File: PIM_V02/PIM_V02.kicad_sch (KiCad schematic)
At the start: 161 parts, among them J1 Conn_01x06, J10 Conn_02x08_Odd_Even, J4 USB_C_Receptacle_USB2.0_14P, J5 Conn_01x04, J6 Conn_01x04, J8 Conn_01x02, J9 Conn_02x08_Odd_Even, Q1 SQJ407EP-T1_GE3, Q2 PMOS, Q3 PMOS, Q4 NMOS, Q5 2N7002, SW1 SW_Push, U1 TPS259541DSGR, U11 AP2112K-3.3, U13 MT29F1G01ABAFDWB-IT_F, U14 MB85RS256B, U15 ICE40UP5K-SG48I, U2 USBLC6-2SC6, U3 STM32H7A3VITx, Y1 Crystal_GND24_Small

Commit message: pc104 outline, nearly done with layout, managed to keep it at 4 layers but the traces became quite messy; still need to do an in depth review to ensure i havent cut across any zones unknowingly; also there are still DRC errors that i need to work through - but all nets are connected !
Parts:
- removed J10, J9: Conn_02x08_Odd_Even, Connector_PinHeader_2.54mm:PinHeader_2x08_P2.54mm_Vertical, symbol Connector_Generic:Conn_02x08_Odd_Even
- removed J8: Conn_01x02, Connector_PinHeader_2.54mm:PinHeader_1x02_P2.54mm_Vertical, symbol Connector_Generic:Conn_01x02
- removed Q5: 2N7002, Package_TO_SOT_SMD:SOT-23, symbol Transistor_FET:2N7002
- removed R57, R58: 4.7kR, Resistor_SMD:R_0603_1608Metric, symbol Device:R_Small
- removed TP10, TP19, TP20, TP9: TestPoint, TestPoint:TestPoint_Pad_D1.0mm, symbol Connector:TestPoint
- removed U1: TPS259541DSGR, CustomFootprints:DSG0008A, symbol Custom_Components:TPS259573DSGR
- added D16: BAS316, Diode_SMD:D_SOD-323, symbol Diode:BAS316
- added J12, J13: Conn_01x12, CustomFootprints:5040501291, symbol Connector_Generic:Conn_01x12
- added J14: Conn_01x04, Connector_Molex:Molex_PicoBlade_53261-0471_1x04-1MP_P1.25mm_Horizontal, symbol Connector_Generic:Conn_01x04
- added R145, R149: 10kR, Resistor_SMD:R_0603_1608Metric, symbol Device:R_Small
- added R146: 33R, Resistor_SMD:R_0402_1005Metric, symbol Device:R_Small
- added R147, R148: 33R, Resistor_SMD:R_0603_1608Metric, symbol Device:R_Small
- added TP21, TP25: TestPoint, TestPoint:TestPoint_Pad_D1.0mm, symbol Connector:TestPoint
- added U1: TPS259540DSGR, CustomFootprints:DSG0008A, symbol Custom_Components:TPS259540DSGR
- R100, R102, R103, R104, R105, R106, R107, R108, R109, R118, R119, R120, R121, R99: footprint Resistor_SMD:R_0603_1608Metric -> Resistor_SMD:R_0402_1005Metric; MPN ERJ-3EKF33R0V -> ERJ-2RKF33R0X; PD RES SMD 33 OHM 1% 1/10W 0603 -> RES SMD 33 OHM 1% 1/10W 0402
- R110, R111, R112, R113, R114, R115, R116, R117, R123, R124, R125, R126, R127: footprint Resistor_SMD:R_0603_1608Metric -> Resistor_SMD:R_0402_1005Metric; MPN ERJ-3EKF4701V -> ERJ-2RKF4701X; PD RES SMD 4.7K OHM 1% 1/10W 0603 -> RES SMD 4.7K OHM 1% 1/10W 0402
- R87: value 1k -> 10kR
- R88: value 100k -> 10kR; MPN (none) -> ERJ-3EKF1002V; PD (none) -> RES SMD 10K OHM 1% 1/10W 0603
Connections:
- net +12V_HK: now also U1.3 (IN), U1.4 (IN)
- net +12V_PL: now also U1.5 (OUT)
- net +3V3_HK: now also R123.2, R145.1; no longer R123.1
- net +3V3_MCU: now also R88.1, R149.1, TP21.1; no longer R59.1
- net BOOT0: now also TP25.1
- net GND: now also R87.2, J12.1 (Pin_1), J12.2 (Pin_2), J12.3 (Pin_3), J12.4 (Pin_4), J13.10 (Pin_10), J13.11 (Pin_11), J13.12 (Pin_12), J13.6 (Pin_6), J13.7 (Pin_7), J13.8 (Pin_8), J13.9 (Pin_9), U1.8 (GND), U1.9 (GND); no longer R88.2
- net OCTOSPI1_BK2_NCS: no longer R59.2
- net PL_IO0: now also J12.5 (Pin_5)
- net PL_IO1: now also J12.6 (Pin_6)
- net PL_IO10: now also J13.3 (Pin_3)
- net PL_IO11: now also J13.4 (Pin_4)
- net PL_IO12: now also J13.5 (Pin_5)
- net PL_IO2: now also J12.7 (Pin_7)
- net PL_IO3: now also J12.8 (Pin_8)
- net PL_IO4: now also J12.9 (Pin_9)
- net PL_IO5: now also J12.10 (Pin_10)
- net PL_IO6: now also J12.11 (Pin_11)
- net PL_IO7: now also J12.12 (Pin_12)
- net PL_IO8: now also R123.1, J13.1 (Pin_1); no longer R123.2
- net PL_IO9: now also J13.2 (Pin_2)
- net SPI4_nSS_FRAM: now also R149.2
- net at C3.2: now also U1.1 (DV_DT)
- net at R5.2: now also U1.7 (ILM)
- net FPGA_TXRDY: now reaches U3.57 (PD10)
- net FPGA_TXRDY: now also U15.4 (IOB_8a)
- net EXTRA_0: now reaches U3.63 (PC6)
- net EXTRA_1: now reaches U3.64 (PC7)
- net at U3.66 (PC9): now also R148.1
- net at U3.67 (PA8): now also R147.1
- net SPI_SCK_CAN2: now reaches U15.13 (IOB_24a)
- net SPI_MOSI_CAN2: now reaches U15.18 (IOB_31b)
- net SPI_MISO_CAN2: now reaches U15.19 (IOB_29b)
- net at U15.20 (IOB_25b_G3): now also R146.2
- net nSS_SPI_CAN2: now reaches U15.21 (IOB_23b)
- net nSS_SPI_CAN2: now also R145.2
- net nINT_CAN2: now reaches U15.6 (IOB_13b)
- net EFUSE_EN renamed EN_EF
- net EN_EF: now also D16.1 (K)
- net EFUSE_ENxxx: no longer names the net of R2.2, R3.1
- net EFUSE_ENxxx: now also D16.2 (A), U1.2 (EN_UVLO)
- net FPGA_EXTRA renamed FPGA_HB
- net I2C2_SCL_PL: no longer names the net of U3.46 (PB10)
- net I2C2_SDA_PL: no longer names the net of U3.47 (PB11)
- net SPI2_MISO_PL: no longer names the net of U3.53 (PB14)
- net SPI2_MOSI_PL: no longer names the net of U3.54 (PB15)
- net SPI2_SCK_PL: no longer names the net of U3.84 (PD3)
- net SPI2_nCS_PL: no longer names the net of U3.85 (PD4)
- net USART3_RX_PL: no longer names the net of U3.56 (PD9)
- net USART3_TX_PL renamed +VARI_ALT
- net +VARI_ALT: now also R88.2
- net nPL_FLT renamed nFLT_EF
- net nFLT_EF: now also U1.6 (nFLT)
- new net CAN2_N: J14.1 (Pin_1), J14.2 (Pin_2)
- new net CAN2_P: J14.3 (Pin_3), J14.4 (Pin_4)
- new net CLKO_CAN2: R146.1
- new net MCO1: R147.2
- new net MCO2: R148.2
- no-connect marks 56 -> 51
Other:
- sheet CAN ports: added CAN2_N, CAN2_P, CLKO_CAN2, SPI_MISO_CAN2, SPI_MOSI_CAN2, SPI_SCK_CAN2, nINT_CAN2, nSS_SPI_CAN2; removed none
- sheet POWER ports: added +VARI_ALT; removed none
- note added: "O/P CONN"
- note added: "One datasheet item to confirm: whether TPS259541DSGR is the latch-off or auto-retry variant, and whether it exposes an IMON (analog current-monitor) pin - the TPS2594 family generally does, and if this variant/package brings it out, you get input current sensing for free."
- note removed: "FPGA CONN"
- note removed: "One datasheet item to confirm: whether TPS259541DSGR is the latch-off or auto-retry variant, and whether it exposes an IMON (analog current-monitor) pin - the TPS2594 family generally does, and if this variant/package brings it out, you get input current sensing for free. I'll verify this from the datasheet next."
- note removed: "PL CONN"
- moved on the sheet: C1, C103, C104, C105, C106, C107, C108, C111, C112, C113, C114, C115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

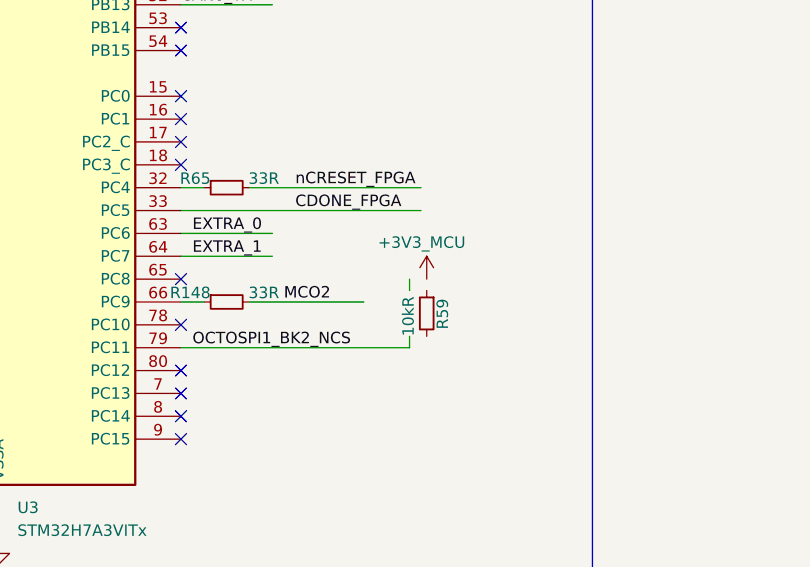
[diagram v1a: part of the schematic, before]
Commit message: No errors, just need to clean up the silkscreen. ready for a review
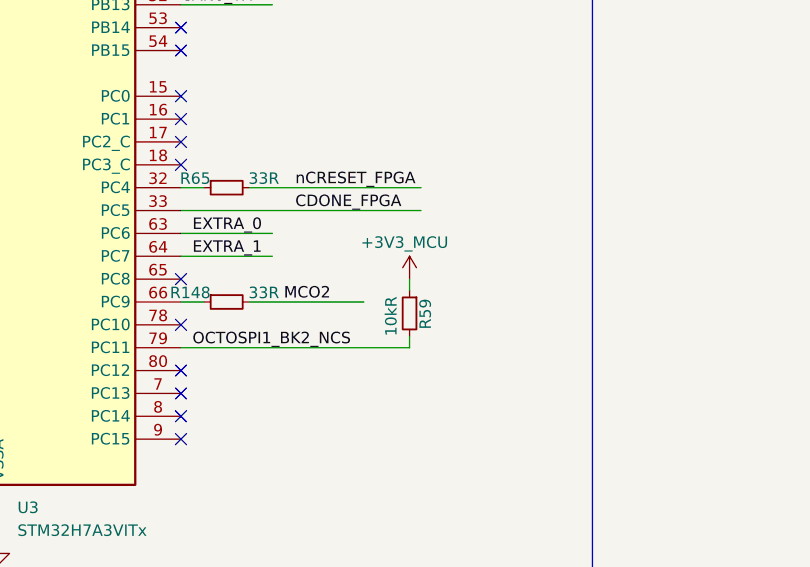
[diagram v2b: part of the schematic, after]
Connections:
- net +3V3_MCU: now also R59.1
- net OCTOSPI1_BK2_NCS: now also R59.2
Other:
- moved on the sheet: R59
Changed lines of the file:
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@@
 	(symbol
 		(lib_id "power:+12V")
-		(at 387.985 144.78 0)
+		(at 386.08 144.78 0)
 		(mirror y)
 		(unit 1)
@@
 		(dnp no)
 		(property "Reference" "#PWR0114"
-			(at 387.985 148.59 0)
+			(at 386.08 148.59 0)
 			(effects
 				(font
@@
 		)
 		(property "Value" "+3V3_MCU"
-			(at 392.303 140.716 0)
+			(at 390.398 140.716 0)
 			(effects
 				(font
@@
 		)
 		(property "Footprint" ""
-			(at 387.985 144.78 0)
+			(at 386.08 144.78 0)
 			(effects
 				(font
@@
 		)
 		(property "Datasheet" ""
-			(at 387.985 144.78 0)
+			(at 386.08 144.78 0)
 			(effects
 				(font
@@
 		)
 		(property "Description" "Power symbol creates a global label with name \"+12V\""
-			(at 387.985 144.78 0)
+			(at 386.08 144.78 0)
 			(effects
 				(font
@@
 	(symbol
 		(lib_id "Device:R_Small")
-		(at 387.985 148.59 0)
+		(at 386.08 148.59 0)
 		(mirror y)
 		(unit 1)
@@
 		(dnp no)
 		(property "Reference" "R59"
-			(at 389.763 150.368 90)
+			(at 387.858 150.368 90)
 			(effects
 				(font
@@
 		)
 		(property "Value" "10kR"
-			(at 385.953 151.13 90)
+			(at 384.048 151.13 90)
 			(effects
 				(font
@@
 		)
 		(property "Footprint" "Resistor_SMD:R_0603_1608Metric"
-			(at 387.985 148.59 0)
+			(at 386.08 148.59 0)
 			(effects
 				(font
@@
 		)
 		(property "Datasheet" "~"
-			(at 387.985 148.59 0)
+			(at 386.08 148.59 0)
 			(effects
 				(font
@@
 		)
 		(property "Description" "Resistor, small symbol"
-			(at 387.985 148.59 0)
+			(at 386.08 148.59 0)
 			(effects
 				(font
@@
 		)
 		(property "MAXIMUM_PACKAGE_HEIGHT" ""
-			(at 387.985 148.59 90)
+			(at 386.08 148.59 90)
 			(effects
 				(font
@@
 		)
 		(property "KLC_S3.3" ""
-			(at 387.985 148.59 90)
+			(at 386.08 148.59 90)
 			(effects
 				(font
@@
 		)
 		(property "KLC_S4.1" ""
-			(at 387.985 148.59 90)
+			(at 386.08 148.59 90)
 			(effects
 				(font
@@
 		)
 		(property "MPN" "ERJ-3EKF1002V"
-			(at 387.985 148.59 90)
+			(at 386.08 148.59 90)
 			(effects
 				(font
@@
 		)
 		(property "PD" "RES SMD 10K OHM 1% 1/10W 0603"
-			(at 387.985 148.59 90)
+			(at 386.08 148.59 90)
 			(effects
 				(font
@@
 		)
 		(property "Note" ""
-			(at 387.985 148.59 90)
-			(effects
-				(font
+			(at 386.08 148.59 90)
+			(effects
+				(font
